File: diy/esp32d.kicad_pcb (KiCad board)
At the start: 2 copper layers, 86.4 x 51.4 mm, 47 parts, among them IC1 CP2102N-A01-GQFN28R, J1 Conn_02x08_Odd_Even, J2 Conn_02x08_Odd_Even, J4 Conn_01x02, Q1 SS8050-G, Q2 SS8050-G, Q3 DMG2307L-7, SW1 SW_Push, U1 AMS1117-3.3, U2 ESP32-WROOM-32D, U3 DizzyBITLogo, U4 MCP73831-2-OT, U5 DizzyBIT-Layout

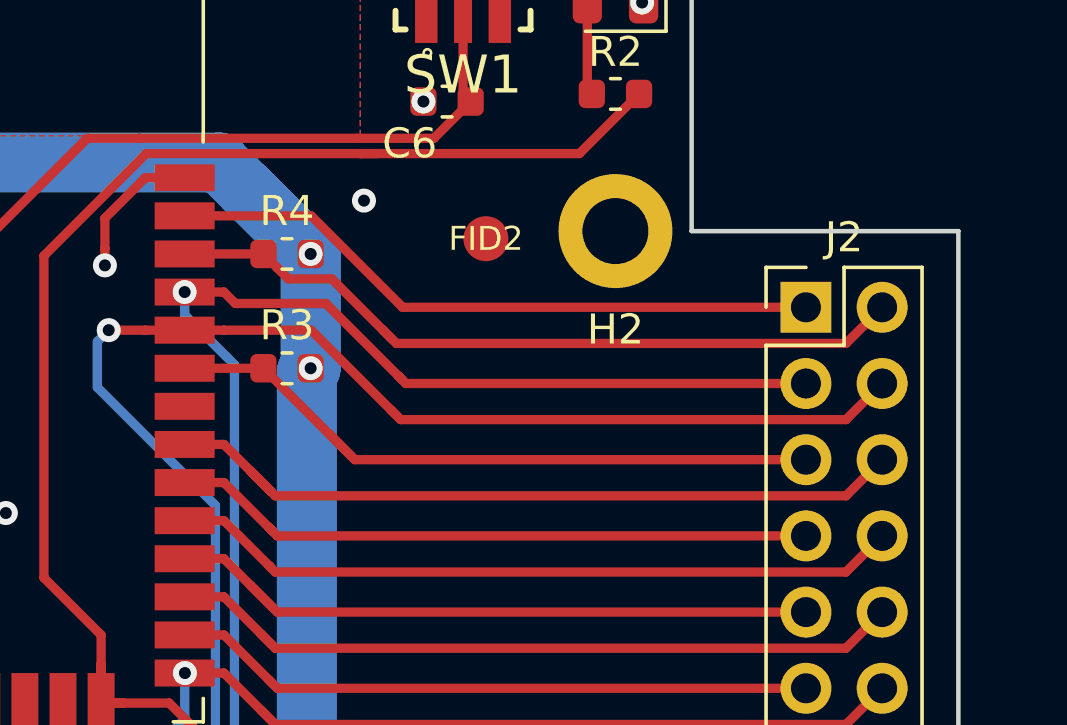
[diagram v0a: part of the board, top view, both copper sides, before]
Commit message: Changed blue led PN for 3.3V
Added DIY project folder
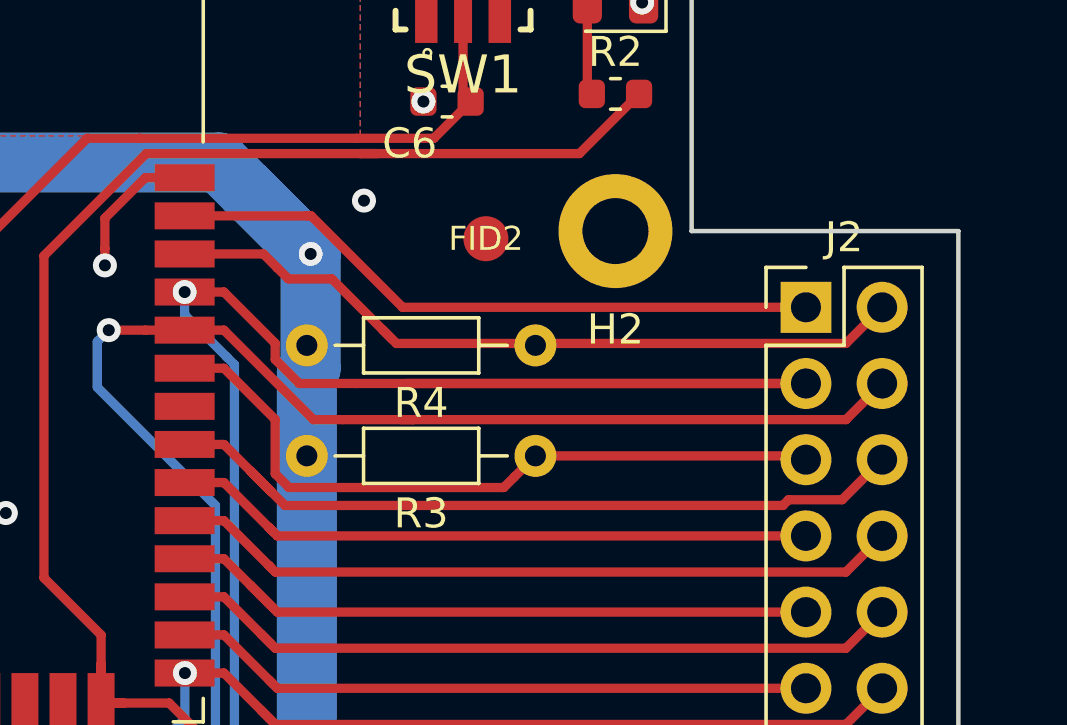
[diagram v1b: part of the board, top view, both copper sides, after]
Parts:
- R3, R4: footprint Resistor_SMD:R_0603_1608Metric -> Resistor_THT:R_Axial_DIN0204_L3.6mm_D1.6mm_P7.62mm_Horizontal
- moved R4 8.82 mm to (134.5, 108.6), turned to 180 degrees
- moved R3 8.78 mm to (134.5, 112.3), turned to 180 degrees
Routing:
- net IO1: track 92.0 -> 105.4 mm
- net I2C_SDA: track 23.1 -> 23.9 mm
- net +3.3V: vias 10 -> 9
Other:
- net class Default: clearance 0.1 -> 0.2
- rule trace_clearance: 0.1 -> 0.2

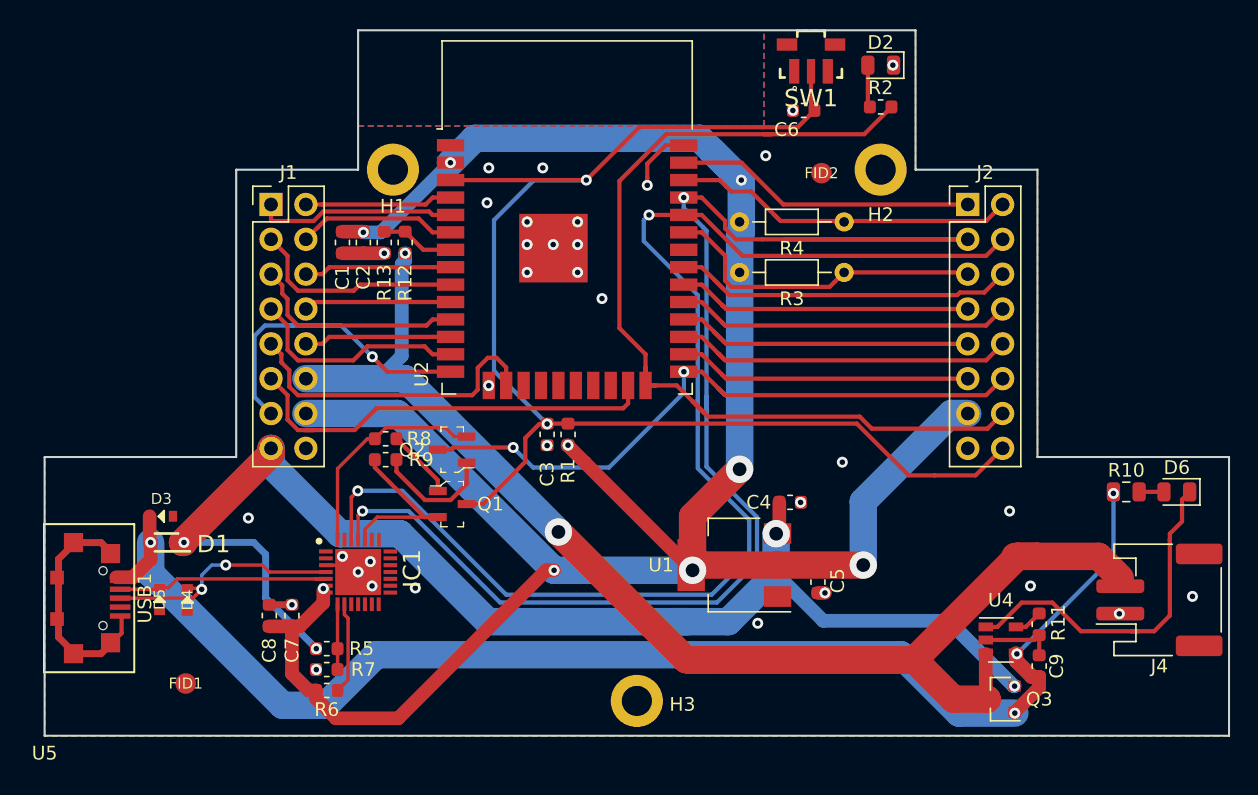
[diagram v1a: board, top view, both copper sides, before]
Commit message: Added DIY board
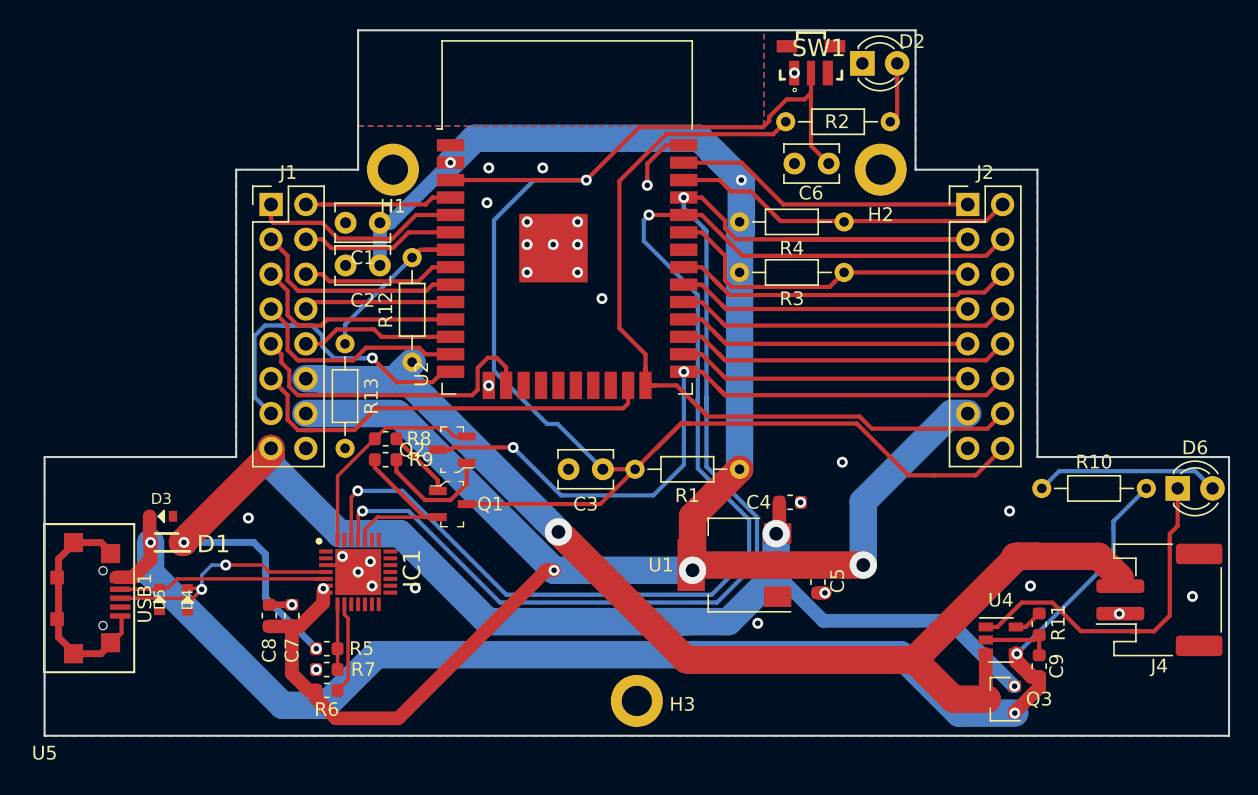
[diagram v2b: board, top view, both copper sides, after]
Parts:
- removed FID1, FID2: FIDUCIAL-1.5mm, fab:FIDUCIAL-1.5mm
- C1, C3, C6: footprint Capacitor_SMD:C_0603_1608Metric -> Capacitor_THT:C_Disc_D3.8mm_W2.6mm_P2.50mm
- C2: value C22uF/10V(20%) -> C22uF/10V(10%); footprint Capacitor_SMD:C_0603_1608Metric -> Capacitor_THT:C_Disc_D3.8mm_W2.6mm_P2.50mm
- D2, D6: footprint LED_SMD:LED_0805_2012Metric -> LED_THT:LED_D3.0mm
- R1, R12, R13, R2: footprint Resistor_SMD:R_0603_1608Metric -> Resistor_THT:R_Axial_DIN0204_L3.6mm_D1.6mm_P7.62mm_Horizontal
- R10: footprint Resistor_SMD:R_0805_2012Metric -> Resistor_THT:R_Axial_DIN0204_L3.6mm_D1.6mm_P7.62mm_Horizontal
- SW1: footprint Button_Switch_SMD:TL3340 -> SamacSys_Parts:TL3340
- moved R1 12.8 mm to (126.9, 126.6), turned to 180 degrees
- moved R12 8.74 mm to (103.0, 118.8)
- moved R13 7.92 mm to (98.1, 117.5)
- moved R2 7.01 mm to (130.2, 101.3), turned to 0 degrees
- moved R10 6.16 mm to (148.9, 128.0), turned to 0 degrees
- moved C3 4.79 mm to (116.9, 126.6), turned to 180 degrees
- moved C6 3.93 mm to (130.9, 104.3)
- moved C1 3.08 mm to (100.6, 108.6), turned to 180 degrees
- moved C2 2.07 mm to (100.6, 111.8), turned to 180 degrees
- moved D2 1.34 mm to (135.8, 97.0), turned to 0 degrees
- moved D6 0.26 mm to (158.8, 128.0), turned to 0 degrees
- moved SW1 0.13 mm to (132.1, 95.6)
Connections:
- C1 pad 1: GND -> +3.3V
- C1 pad 2: +3.3V -> GND
- C3 pad 1: GND -> EN
- C3 pad 2: EN -> GND
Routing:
- net EN: track 101.2 -> 117.6 mm, vias 2 -> 1
- net +3.3V: track 173.8 -> 161.0 mm, vias 9 -> 6
- net Net-(D6-Pad2): track 1.81 -> 13.5 mm
- net IO2: track 69.5 -> 60.7 mm
- net I35: track 5.38 -> 13.3 mm
- net IO0: track 47.5 -> 52.3 mm
- net GND: track 35.6 -> 32.4 mm, vias 34 -> 30
- net VBAT: track 115.0 -> 112.1 mm, vias 2 -> 1
- net HSPI_MISO: track 22.6 -> 24.5 mm
- net VBUS: track 102.7 -> 104.1 mm, vias 4 -> 3
- net Net-(D2-Pad2): track 3.11 -> 4.46 mm
- net I39: track 14.7 -> 15.5 mm

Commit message: Finished the DIY board
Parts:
- removed C7: C4.7uF/6.3V(20%), Capacitor_SMD:C_0603_1608Metric
- removed C8: C0.1uF/50V(10%), Capacitor_SMD:C_0603_1608Metric
- removed D1: BAT760,115, SOD2513X120N
- removed D3, D4, D5: T5V0S5-7, smd-semi:SOD-523
- removed IC1: CP2102N-A01-GQFN28R, SamacSys_Parts:QFN50P500X500X80-29N-D
- removed R5: R22.1K(1%), Capacitor_SMD:C_0603_1608Metric
- removed R6: R2Kohm(5%), Resistor_SMD:R_0603_1608Metric
- removed R7: R47.5K(1%), Capacitor_SMD:C_0603_1608Metric
- removed USB1: USB_B_Micro, Connfly:DS1105-12
- added H4: MountingHole_Pad, MountingHole:MountingHole_2.2mm_M2_DIN965_Pad, F.Cu at (113.2, 110.5)
- added U6: DizzyBit-MicroUSB-UART, DizzyBit:DizzyBit-MicroUSB-UART, F.Cu at (76.4, 128.3)
- C4, C5: value C22uF/10V(20%) -> C22uF/10V(10%); footprint Capacitor_SMD:C_0603_1608Metric -> Capacitor_THT:C_Disc_D3.8mm_W2.6mm_P2.50mm
- C9: footprint Capacitor_SMD:C_0603_1608Metric -> Capacitor_THT:C_Disc_D3.8mm_W2.6mm_P2.50mm
- J4: footprint Connector_JST:JST_PH_S2B-PH-SM4-TB_1x02-1MP_P2.00mm_Horizontal -> Connector_JST:JST_PH_S2B-PH-K_1x02_P2.00mm_Horizontal
- Q1, Q2: value SS8050-G -> SS8050DTA; footprint digikey-footprints:SOT-23-3 -> Package_TO_SOT_THT:TO-92_Inline_Wide
- Q3: footprint Package_TO_SOT_SMD:SOT-23 -> Package_TO_SOT_SMD:SOT-23W_Handsoldering
- R11, R8, R9: footprint Resistor_SMD:R_0603_1608Metric -> Resistor_THT:R_Axial_DIN0204_L3.6mm_D1.6mm_P7.62mm_Horizontal
- SW1: footprint SamacSys_Parts:TL3340 -> Button_Switch_SMD:TL3340-HandSoldering
- U1: footprint Package_TO_SOT_SMD:SOT-223-3_TabPin2 -> Package_TO_SOT_SMD:SOT-223-3_TabPin2-HandSoldering
- U4: footprint Package_TO_SOT_SMD:SOT-23-5 -> Package_TO_SOT_SMD:SOT-23-5_HandSoldering
- moved R8 15.5 mm to (103.4, 139.7), turned to 90 degrees
- moved R11 9.91 mm to (148.9, 128.0), turned to 0 degrees
- moved C9 7.67 mm to (155.9, 143.7)
- moved R9 7.67 mm to (105.6, 132.1), turned to 270 degrees
- moved Q2 7.54 mm to (110.9, 130.9), turned to 0 degrees
- moved C3 6.27 mm to (122.6, 123.9)
- moved U4 4.04 mm to (145.0, 135.1)
- moved C5 3.53 mm to (135.9, 133.6), turned to 0 degrees
- moved C2 2.54 mm to (98.1, 112.2), turned to 0 degrees
- moved R10 2.50 mm to (148.9, 130.5)
- moved Q1 2.27 mm to (103.7, 128.9)
- moved J4 1.49 mm to (156.2, 136.9)
- moved C4 1.00 mm to (131.2, 128.3), turned to 90 degrees
- moved D2 0.81 mm to (135.8, 97.8)
- moved SW1 0.27 mm to (131.8, 95.6)
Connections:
- Q2 pad 2: DTR -> IO0
- Q2 pad 3: IO0 -> DTR
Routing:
- net GND: track 32.4 -> 4.90 mm, vias 30 -> 7
- net DTR: track 15.8 -> 40.0 mm
- net VBAT: track 112.1 -> 93.6 mm, vias 1 -> 2
- net USB_DP: track 17.8 -> 0.00 mm, vias 2 -> 0
- net USB_DN: track 16.0 -> 0.00 mm
- net EXT_5V: track 101.7 -> 87.7 mm
- net EN: track 117.6 -> 103.7 mm
- net IO1: track 105.4 -> 116.1 mm
- net Net-(R11-Pad2): track 2.10 -> 12.7 mm
- net VBUS: track 104.1 -> 95.1 mm, vias 3 -> 2
- net Net-(D6-Pad1): track 26.0 -> 18.6 mm
- net IO3: track 94.6 -> 101.8 mm
- net Net-(IC1-Pad9): track 6.71 -> 0.00 mm
- net Net-(IC1-Pad8): track 4.76 -> 0.00 mm
- net RTS: track 13.1 -> 17.1 mm
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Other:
- board text added: "ESP32D DIY MCU"
- board text removed: "ESP32D MCU"
